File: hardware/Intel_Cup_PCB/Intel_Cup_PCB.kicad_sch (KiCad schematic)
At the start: 23 parts

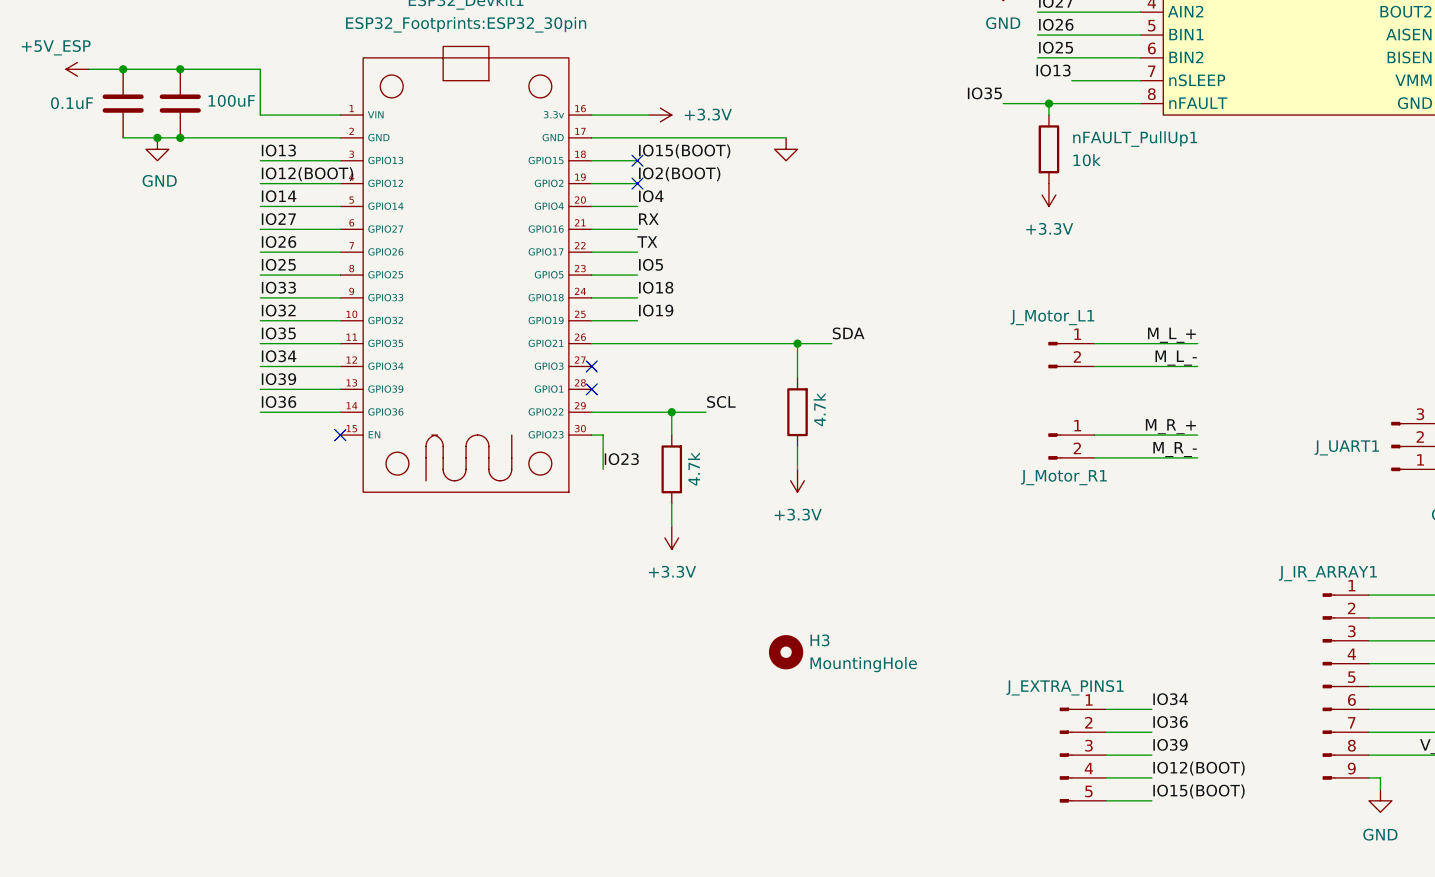
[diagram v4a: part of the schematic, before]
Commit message: Added bump sensor and distance sensor footprints
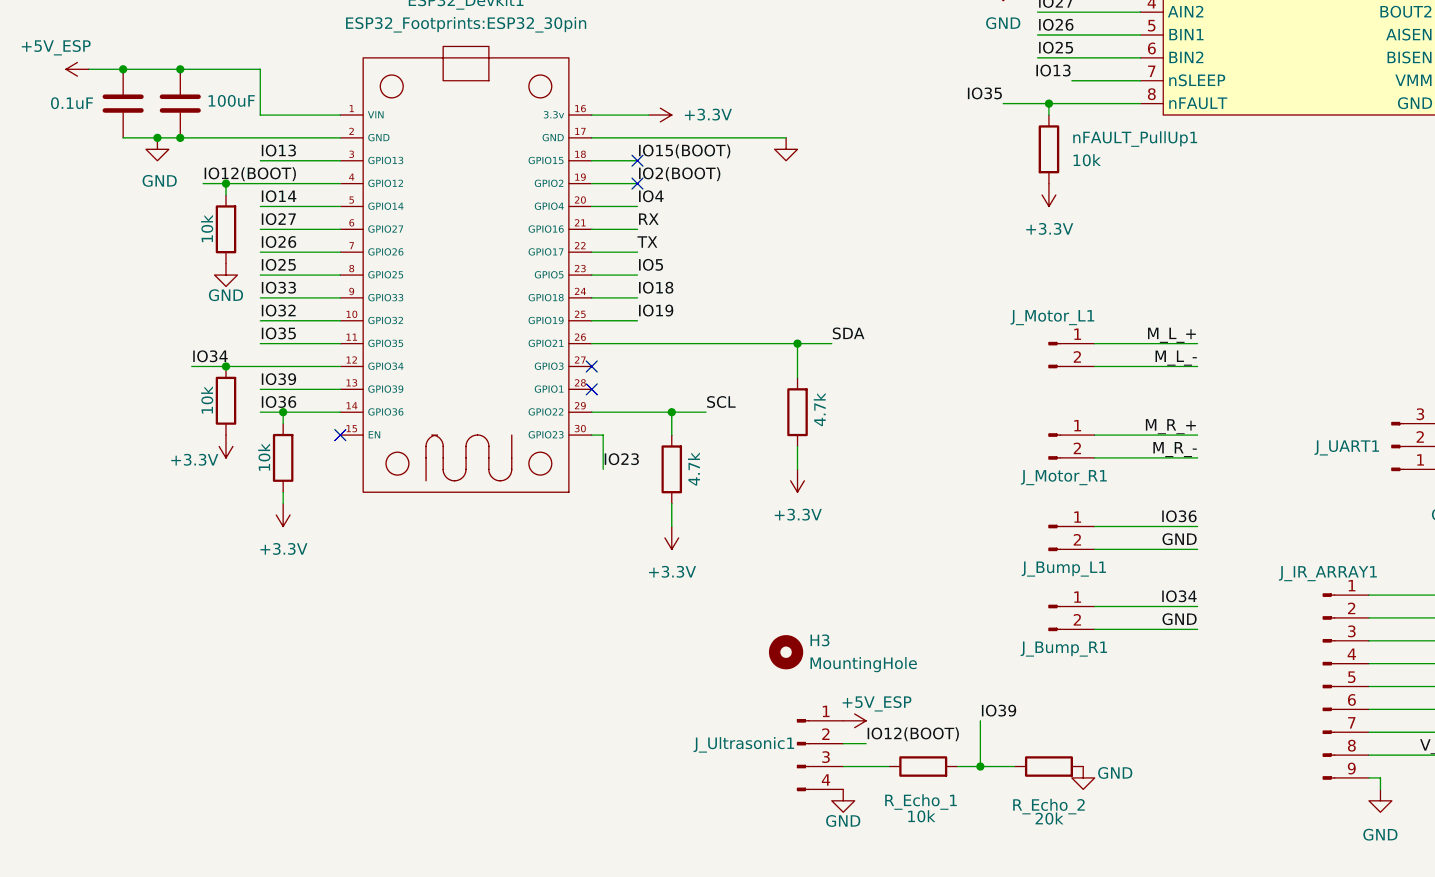
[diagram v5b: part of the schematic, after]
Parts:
- removed J_EXTRA_PINS1: Conn_01x05_Pin, Connector_PinSocket_2.54mm:PinSocket_1x05_P2.54mm_Vertical, symbol Connector:Conn_01x05_Pin
- added J_Bump_L1, J_Bump_R1: Conn_01x02_Pin, Connector_PinHeader_2.54mm:PinHeader_1x02_P2.54mm_Vertical, symbol Connector:Conn_01x02_Pin
- added J_Ultrasonic1: (no value), Connector_PinSocket_2.54mm:PinSocket_1x04_P2.54mm_Vertical, symbol Connector:Conn_01x04_Pin
- added R_Bump_L1, R_Bump_R1, R_Echo_1, R_Trig_Pulldown1: 10k, Resistor_THT:R_Axial_DIN0207_L6.3mm_D2.5mm_P7.62mm_Horizontal, symbol Device:R
- added R_Echo_2: 20k, Resistor_THT:R_Axial_DIN0207_L6.3mm_D2.5mm_P7.62mm_Horizontal, symbol Device:R
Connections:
- net +3.3V: now also R_Bump_L1.1, R_Bump_R1.1
- net +5V_ESP: now also J_Ultrasonic1.1 (Pin_1)
- net GND: now also J_Bump_L1.2 (Pin_2), J_Bump_R1.2 (Pin_2), J_Ultrasonic1.4 (Pin_4), R_Echo_2.2, R_Trig_Pulldown1.1
- net IO12(BOOT): now also J_Ultrasonic1.2 (Pin_2), R_Trig_Pulldown1.2
- net IO34: now also J_Bump_R1.1 (Pin_1), R_Bump_R1.2
- net IO36: now also J_Bump_L1.1 (Pin_1), R_Bump_L1.2
- net IO39: now also R_Echo_1.2, R_Echo_2.1
- new net: J_Ultrasonic1.3 (Pin_3), R_Echo_1.1

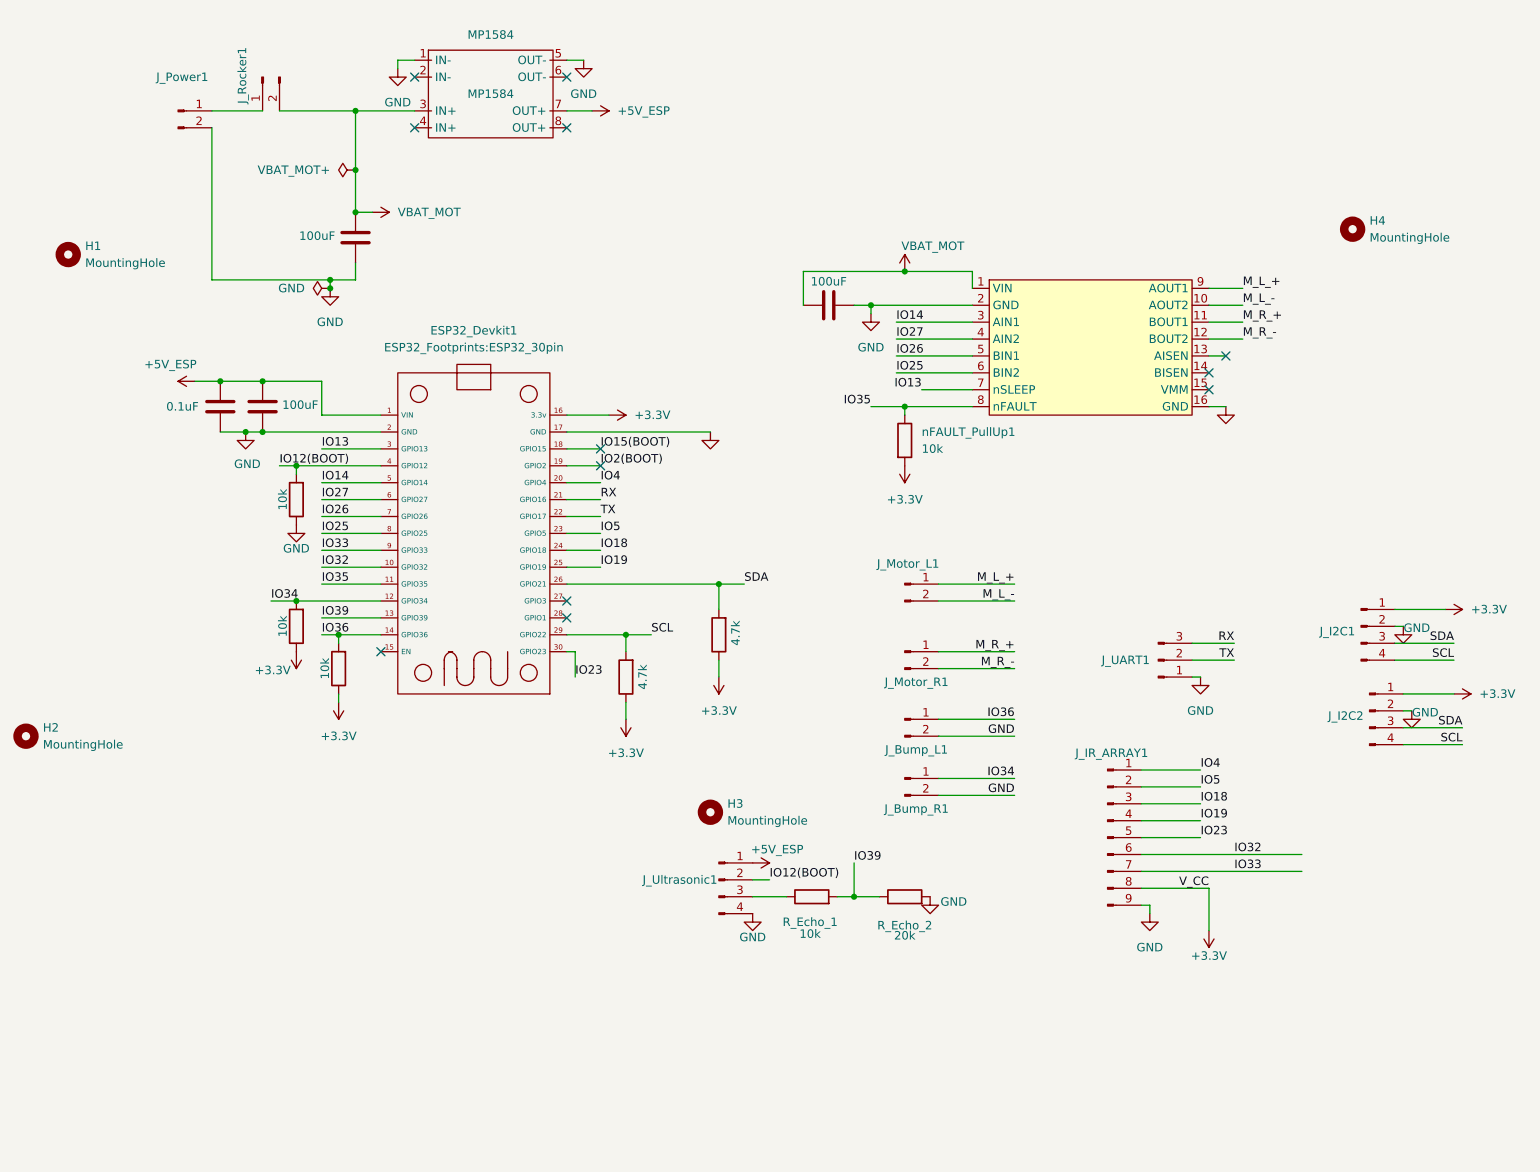
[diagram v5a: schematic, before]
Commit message: Completed PCB with better ESP32 placement
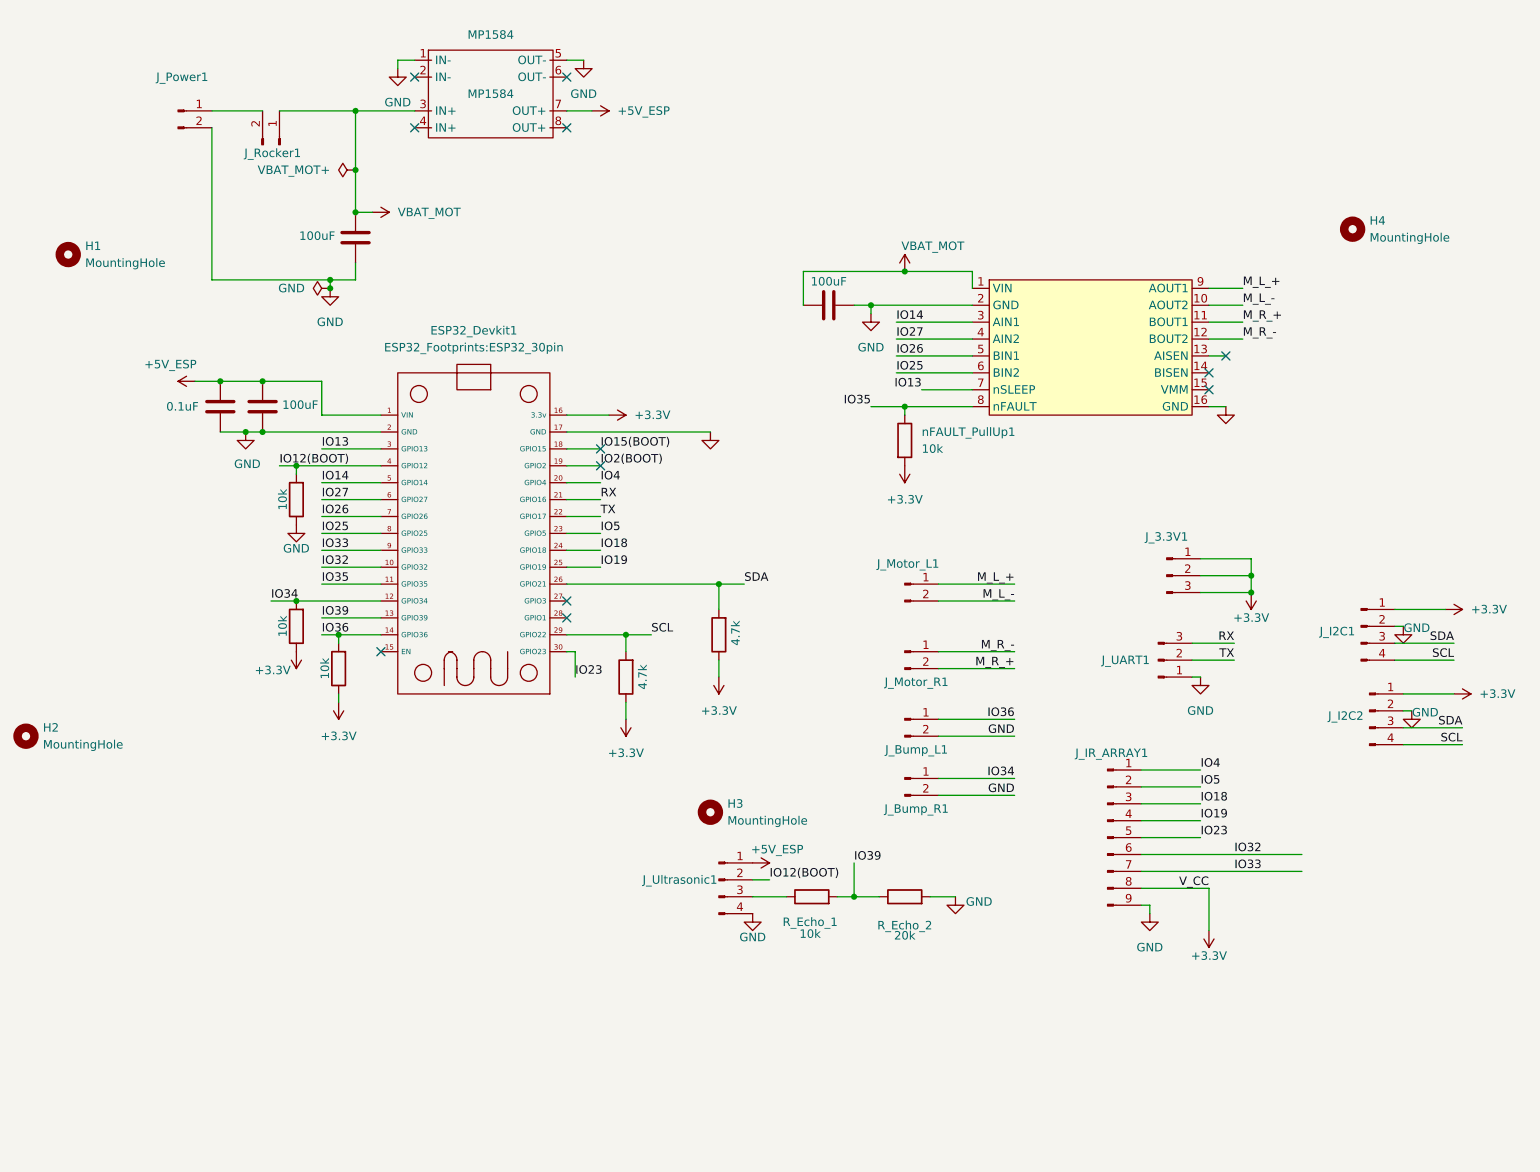
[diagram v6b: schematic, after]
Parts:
- added J_3.3V1: Conn_01x03_Pin, Connector_PinHeader_2.54mm:PinHeader_1x03_P2.54mm_Vertical, symbol Connector:Conn_01x03_Pin
- renumbered R_SCL_Pullup_DNP1 to R_SCL_DNP1, R_SDA_Pullup_DNP1 to R_SDA_DNP1
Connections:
- net +3.3V: now also J_3.3V1.1 (Pin_1), J_3.3V1.2 (Pin_2), J_3.3V1.3 (Pin_3)
- net M_R_+: now also J_Motor_R1.2 (Pin_2); no longer J_Motor_R1.1 (Pin_1)
- net M_R_-: now also J_Motor_R1.1 (Pin_1); no longer J_Motor_R1.2 (Pin_2)
- net VBAT_MOT: now also J_Rocker1.1 (Pin_1); no longer J_Rocker1.2 (Pin_2)
- net at J_Power1.1 (Pin_1): now also J_Rocker1.2 (Pin_2); no longer J_Rocker1.1 (Pin_1)
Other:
- moved on the sheet: J_Rocker1
